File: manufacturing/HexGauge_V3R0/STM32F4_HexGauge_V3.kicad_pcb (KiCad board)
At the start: 4 copper layers, 49.8 x 44.2 mm, 66 parts, among them J1 USB_B_Micro, J2 Conn_ARM_SWD_TC2030-NL, J3 Micro_SD_Card, J4 Conn_01x04_Pin, Q1 Q_PMOS_GSD, SW1 SW_SPDT, SW2 SW_Omron_B3FS, U1 STM32F405RGT6, U2 TPMP2359D, U3 SN65HVD230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

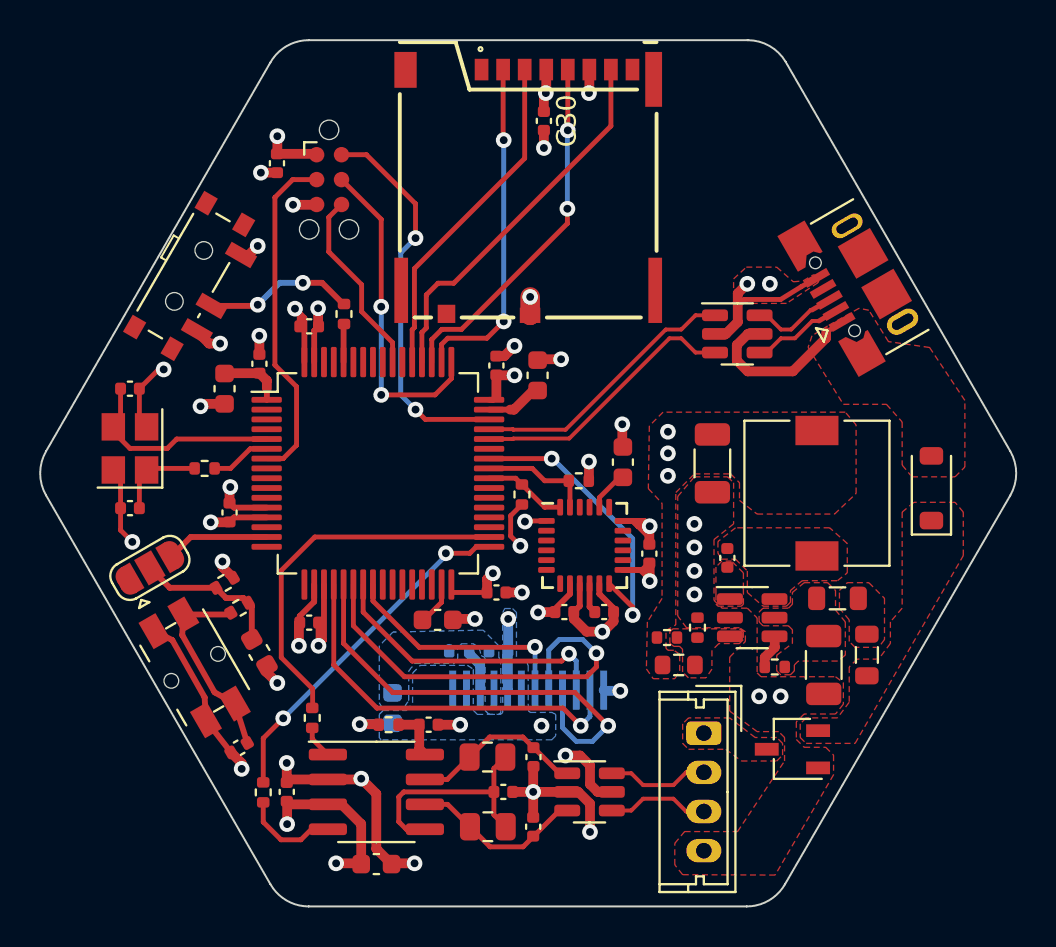
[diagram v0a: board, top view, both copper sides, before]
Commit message: Updated Board
Added Mounting Hole and 3D Packages
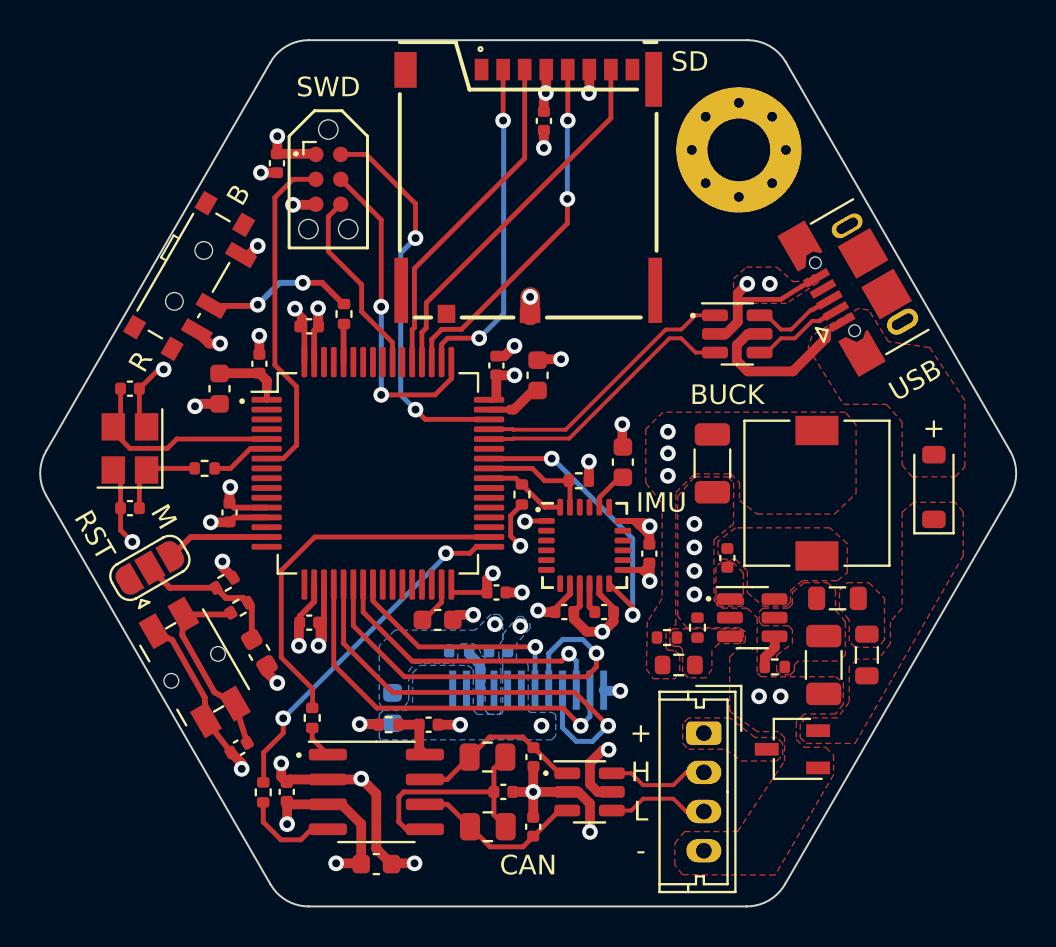
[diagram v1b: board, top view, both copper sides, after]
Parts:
- added H2: MountingHole, MountingHole:MountingHole_3.2mm_M3_Pad_Via, F.Cu at (132.7, 67.3)
- moved C1 0.26 mm to (106.2, 79.5)
- moved D1 0.14 mm to (142.6, 84.5)
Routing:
- net GND: track 92.0 -> 88.4 mm
- net +3V3: track 50.2 -> 50.3 mm, vias 19 -> 20
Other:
- board text added: "+"
- board text added: "-"
- board text added: "B"
- board text added: "BUCK"
- board text added: "CAN"
- board text added: "H"
- board text added: "IMU"
- board text added: "L"
- board text added: "M"
- board text added: "R"
- board text added: "RST"
- board text added: "SD"
- board text added: "SWD"
- board text added: "USB"

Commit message: Updated Board and added Images
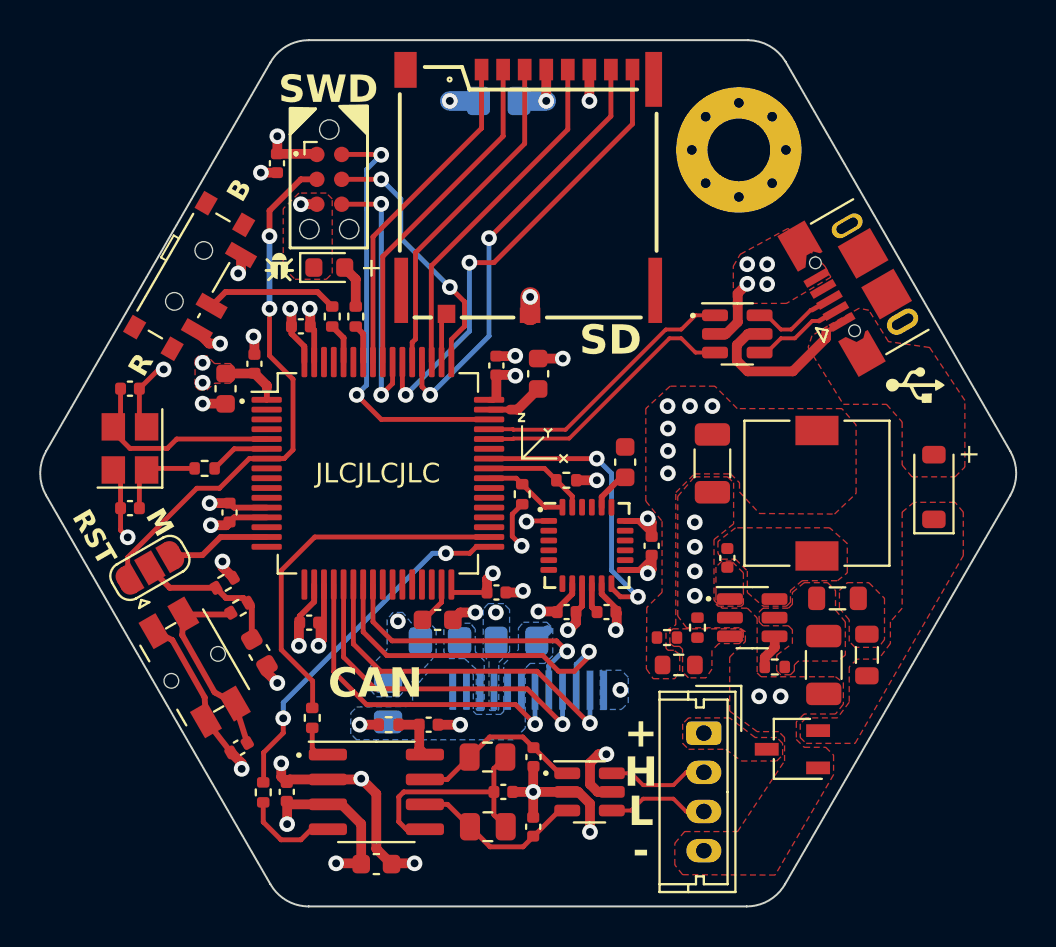
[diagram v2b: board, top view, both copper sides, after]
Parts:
- added D2: White, LED_SMD:LED_0603_1608Metric, F.Cu at (111.8, 73.3)
- added G***: LOGO, Symbol:Gyro_Logo, F.Cu at (122.7, 82.1)
- added G***: LOGO, Symbol:USB_Logo_1mm, F.Cu at (141.7, 79.3)
- added G***: LOGO, Symbol:Bug_Logo, F.Cu at (109.2, 73.3)
- added G***: LOGO, Symbol:GitHubQR_Logo, B.Cu at (137.4, 83.8)
- added R9: 1k5, Resistor_SMD:R_0402_1005Metric, F.Cu at (113.1, 75.8)
- C25: footprint Capacitor_SMD:C_0402_1005Metric -> Capacitor_SMD:C_0805_2012Metric_Pad1.18x1.45mm_HandSolder
- C26: footprint Capacitor_SMD:C_0603_1608Metric -> Capacitor_SMD:C_0805_2012Metric_Pad1.18x1.45mm_HandSolder
- C30: footprint Capacitor_SMD:C_0402_1005Metric -> Capacitor_SMD:C_0805_2012Metric_Pad1.18x1.45mm_HandSolder; moved to B.Cu
- R15: footprint Resistor_SMD:R_0402_1005Metric -> Resistor_SMD:R_0805_2012Metric_Pad1.20x1.40mm_HandSolder
- moved C30 2.52 mm to (120.4, 64.8), turned to 180 degrees
- moved R15 1.11 mm to (117.4, 92.4)
- moved C25 1.06 mm to (121.3, 92.4)
- moved R3 0.63 mm to (123.9, 84.2)
- moved R1 0.62 mm to (111.9, 75.8)
- moved C3 0.42 mm to (110.3, 76.3)
- moved C18 0.42 mm to (128.2, 87.5)
- moved C26 0.40 mm to (114.8, 95.5)
- moved C1 0.31 mm to (106.5, 79.5)
- moved C2 0.25 mm to (108.0, 78.2)
- moved C17 0.12 mm to (123.9, 90.9)
- moved C23 0.12 mm to (125.9, 90.9)
- moved C24 0.12 mm to (126.9, 83.2)
- moved U5 0.12 mm to (124.9, 87.5)
- moved C10 0.08 mm to (122.4, 78.7)
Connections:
- net Net-(H1-LEDA) renamed /Connectors/TFT_LEDA
- net SD_MISO renamed SD_DAT0
- net SD_MOSI renamed SD_CMD
- net SD_SCK renamed SD_CLK
- J3 pad 1: unconnected-(J3-DAT2-Pad1) -> SD_DAT2
- J3 pad 2: SD_CS -> SD_DAT3
- J3 pad 8: unconnected-(J3-DAT1-Pad8) -> SD_DAT1
- J3 pad 9: SD_CD -> SD_DET
- U1 pad 20: TFT_RST -> TFT_DC
- U1 pad 22: TFT_CS -> TFT_RST
- U1 pad 24: TFT_DC -> TFT_CS
- U1 pad 50: SD_CS -> SD_DET
- U1 pad 54: unconnected-(U1-PD2-Pad54) -> SD_DAT1
- U1 pad 56: unconnected-(U1-PB4-Pad56) -> SD_DAT3
- U1 pad 57: unconnected-(U1-PB5-Pad57) -> SD_DAT2
- U1 pad 58: unconnected-(U1-PB6-Pad58) -> /MCU/DEBUG_LED
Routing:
- net SD_DAT1: track 0.00 -> 23.9 mm, vias 0 -> 2
- net SD_DAT3: track 0.00 -> 17.5 mm
- net SD_DAT2: track 0.00 -> 17.2 mm
- net SD_CS: track 17.2 -> 0.00 mm, vias 2 -> 0
- net GND: track 88.4 -> 76.4 mm
- net NRST: track 17.4 -> 27.7 mm, vias 0 -> 2
- net TFT_CS: track 21.4 -> 14.9 mm
- net TFT_DC: track 12.3 -> 17.6 mm
- net TFT_SCK: track 23.1 -> 18.0 mm
- net SWO: track 9.68 -> 13.7 mm, vias 0 -> 2
- net SD_DAT0: track 18.9 -> 22.3 mm, vias 0 -> 2
- net SWCLK: track 16.6 -> 13.4 mm
- net SD_DET: track 0.00 -> 2.58 mm
- net TFT_MOSI: track 15.1 -> 17.6 mm
- net /Connectors/TFT_LEDA: track 2.21 -> 0.00 mm
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- added copper zone on B.Cu, net /Connectors/TFT_LEDA
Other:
- board text added: "JLCJLCJLC"
- board text removed: "BUCK"
- board text removed: "IMU"
- board text removed: "USB"

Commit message: V3R0 SPI SD Card Update
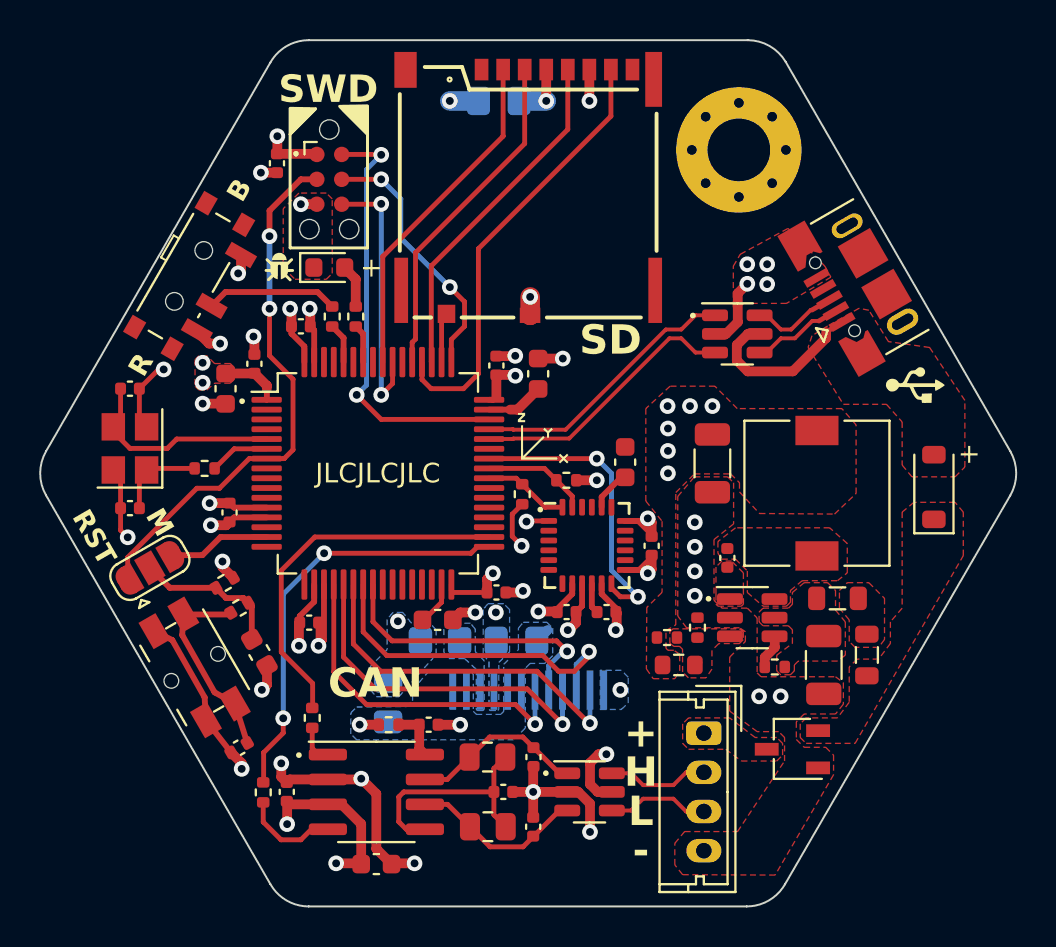
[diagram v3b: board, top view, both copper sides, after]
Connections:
- J3 pad 1: SD_DAT2 -> unconnected-(J3-DAT2-Pad1)
- J3 pad 8: SD_DAT1 -> unconnected-(J3-DAT1-Pad8)
- U1 pad 54: SD_DAT1 -> unconnected-(U1-PD2-Pad54)
- U1 pad 57: SD_DAT2 -> unconnected-(U1-PB5-Pad57)
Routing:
- net SD_DAT1: track 23.9 -> 0.00 mm, vias 2 -> 0
- net SD_DAT2: track 17.2 -> 0.00 mm
- net CAN_RX: track 18.3 -> 21.5 mm
- net SD_DAT0: track 22.3 -> 22.6 mm, vias 2 -> 0
